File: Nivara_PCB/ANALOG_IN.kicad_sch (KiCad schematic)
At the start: 0 parts

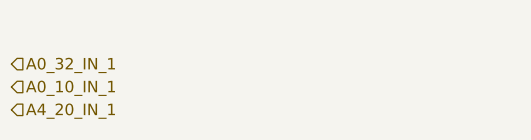
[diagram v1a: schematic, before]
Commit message: Añadido de funciones NPN/PNP
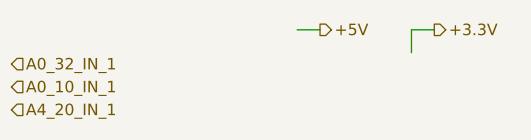
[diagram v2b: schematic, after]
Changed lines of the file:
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@@
 	(generator_version "9.0")
 	(paper "A4")
+	(wire
+		(pts
+			(xy 86.36 52.07) (xy 88.9 52.07)
+		)
+		(stroke
+			(width 0)
+			(type default)
+		)
+	)
+	(wire
+		(pts
+			(xy 101.6 52.07) (xy 99.06 52.07)
+		)
+		(stroke
+			(width 0)
+			(type default)
+		)
+	)
+	(wire
+		(pts
+			(xy 99.06 52.07) (xy 99.06 54.61)
+		)
+		(stroke
+			(width 0)
+			(type default)
+		)
+	)
+	(hierarchical_label "+3.3V"
+		(shape output)
+		(at 101.6 52.07 0)
+		(effects
+			(font
+				(size 1.27 1.27)
+			)
+			(justify left)
+		)
+	)
+	(hierarchical_label "+5V"
+		(shape output)
+		(at 88.9 52.07 0)
+		(effects
+			(font
+				(size 1.27 1.27)
+			)
+			(justify left)
+		)
+	)
 	(hierarchical_label "A4_20_IN_1"
 		(shape input)

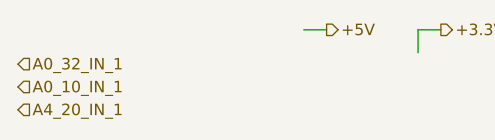
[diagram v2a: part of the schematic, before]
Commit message: Cambios en el esquema de NPN y PNP
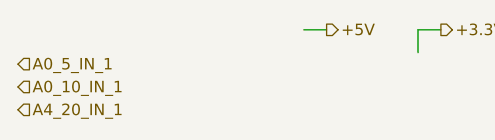
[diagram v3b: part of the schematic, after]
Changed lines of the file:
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@@
 		)
 	)
-	(hierarchical_label "A0_32_IN_1"
+	(hierarchical_label "A0_5_IN_1"
 		(shape input)
 		(at 54.61 55.88 0)

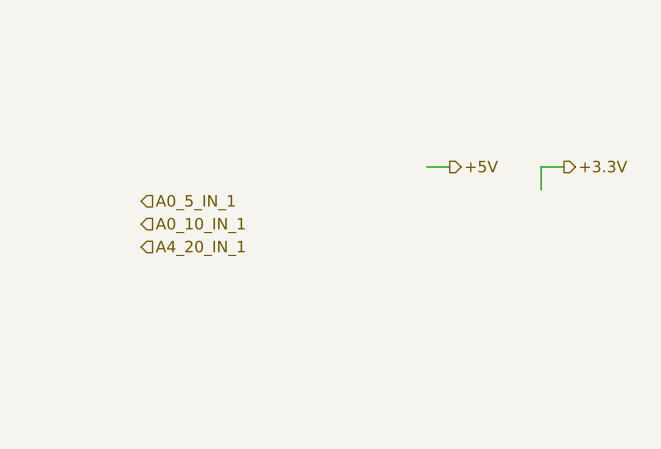
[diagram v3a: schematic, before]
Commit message: Cambios en las mediciones análogas.
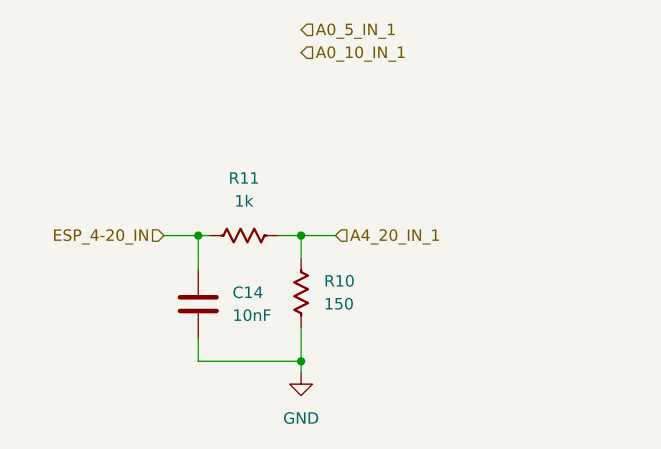
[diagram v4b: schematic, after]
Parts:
- added C14: 10nF, PCM_Capacitor_SMD_AKL:C_0603_1608Metric, symbol PCM_Capacitor_US_AKL:C_0603
- added R10: 150, PCM_Resistor_SMD_AKL:R_0805_2012Metric, symbol PCM_Resistor_US_AKL:R_0805
- added R11: 1k, PCM_Resistor_SMD_AKL:R_0603_1608Metric, symbol PCM_Resistor_US_AKL:R_0603
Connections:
- net A4_20_IN_1: now also R10.1, R11.2
- new net ESP_4-20_IN: C14.1, R11.1
- new net GND: C14.2, R10.2

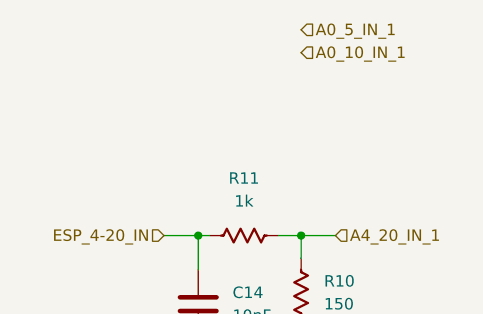
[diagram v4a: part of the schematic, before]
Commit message: Cambios en las salidas analogicas, ya que el ESP32 S3 no tiene DAC
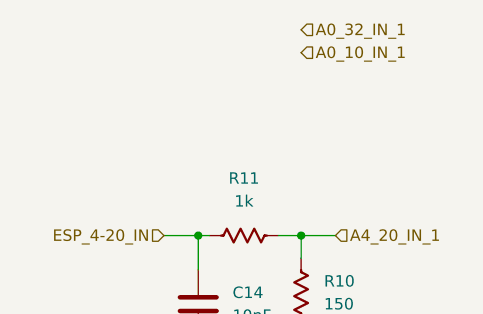
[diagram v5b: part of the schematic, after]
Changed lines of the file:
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@@
 		)
 	)
-	(hierarchical_label "A0_5_IN_1"
+	(hierarchical_label "A0_32_IN_1"
 		(shape input)
 		(at 72.39 36.83 0)

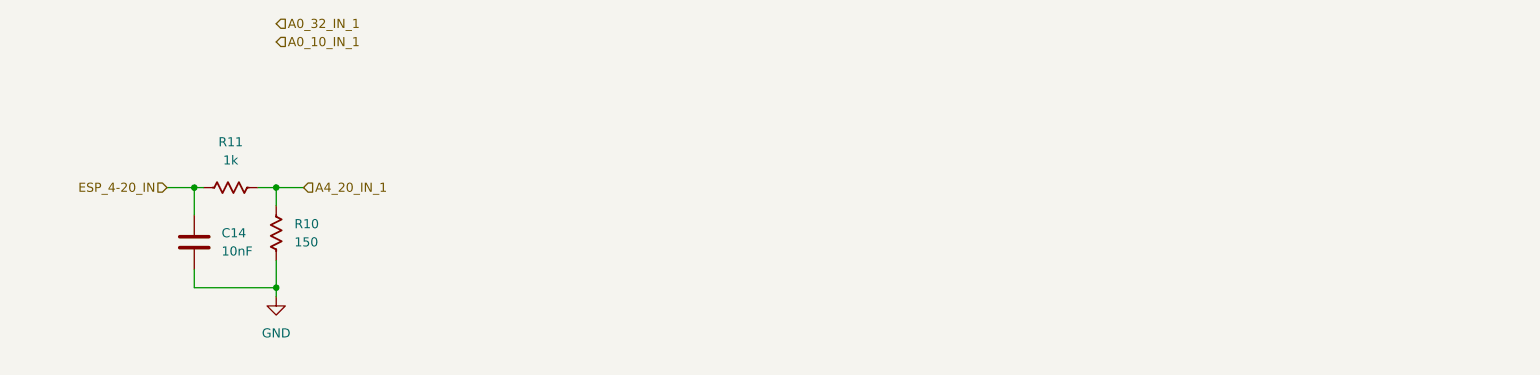
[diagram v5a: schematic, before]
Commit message: Cambios en la medición de voltaje y corriente de la PCB Nivara.
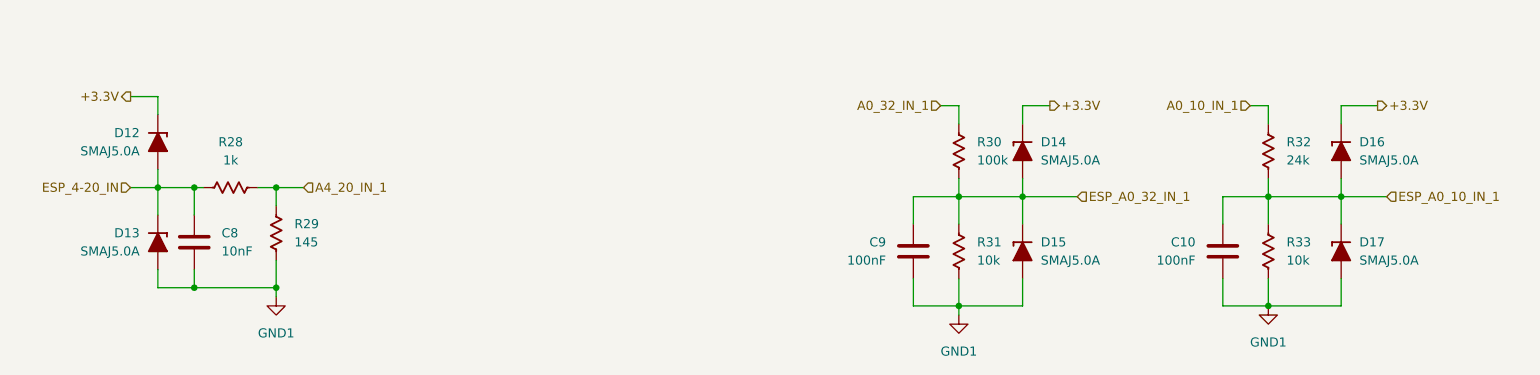
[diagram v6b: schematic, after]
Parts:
- added C10, C9: 100nF, PCM_Capacitor_SMD_AKL:C_0603_1608Metric, symbol PCM_Capacitor_US_AKL:C_0603
- added D12, D13, D14, D15, D16, D17: SMAJ5.0A, PCM_Diode_SMD_AKL:D_SMA, symbol PCM_Diode_TVS_AKL:SMAJ5.0A
- added R30: 100k, PCM_Resistor_SMD_AKL:R_0603_1608Metric, symbol PCM_Resistor_US_AKL:R_0603
- added R31, R33: 10k, PCM_Resistor_SMD_AKL:R_0603_1608Metric, symbol PCM_Resistor_US_AKL:R_0603
- added R32: 24k, PCM_Resistor_SMD_AKL:R_0603_1608Metric, symbol PCM_Resistor_US_AKL:R_0603
- C8: renamed from C14; Voltage (none) -> 10V
- R29: renamed from R10; value 150 -> 145
- renumbered R11 to R28
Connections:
- net A0_10_IN_1: now also R32.2
- net A0_32_IN_1: now also R30.2
- net ESP_4-20_IN: now also D12.2 (A), D13.1 (K)
- net GND renamed GND1
- net GND1: now also C10.2, C9.2, D13.2 (A), D15.2 (A), D17.2 (A), R31.1, R33.1
- new net +3.3V: D12.1 (K), D14.1 (K), D16.1 (K)
- new net ESP_A0_10_IN_1: C10.1, D16.2 (A), D17.1 (K), R32.1, R33.2
- new net ESP_A0_32_IN_1: C9.1, D14.2 (A), D15.1 (K), R30.1, R31.2

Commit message: Cambios en el PCB de Nivara. Ruteo de emtradas y salidas NPN y PNP.
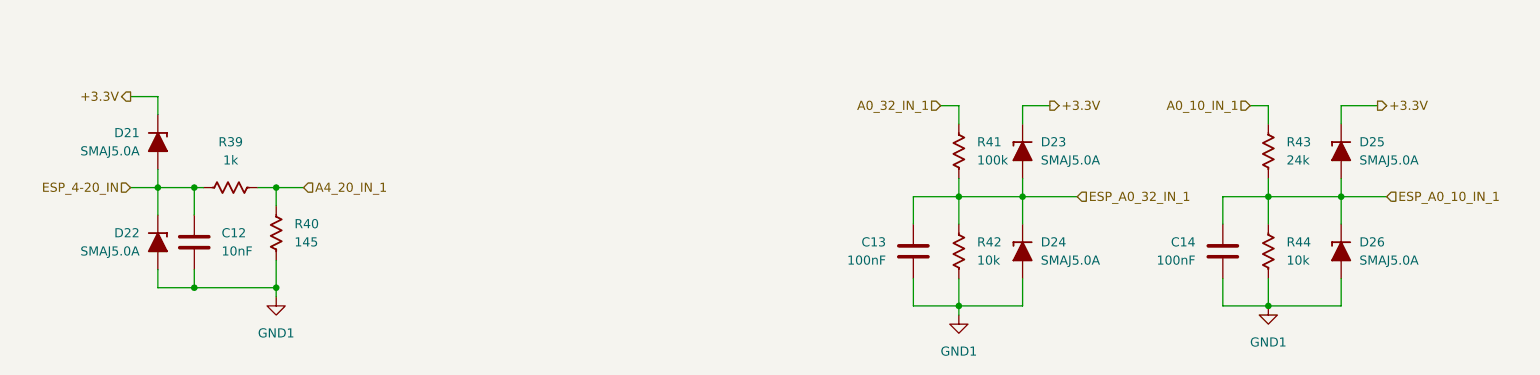
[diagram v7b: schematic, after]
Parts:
- renumbered C8 to C12, C9 to C13, C10 to C14, D12 to D21, D13 to D22, D14 to D23, D15 to D24, D16 to D25, D17 to D26, R28 to R39, R29 to R40, R30 to R41, R31 to R42, R32 to R43, R33 to R44
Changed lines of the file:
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@@
 		(dnp no)
 		(fields_autoplaced yes)
-		(property "Reference" "D17"
+		(property "Reference" "D26"
 			(at 223.52 67.3099 90)
 			(effects
@@
 			(project "Nivara_PCB"
 				(path "/13184db0-a71d-4054-b13a-bbf46d2b100d/4e7fa7f2-8bf5-4f9c-874d-fa1b4fd76f92/20ba0c48-a9e2-46df-b6c2-3a15a589565c"
-					(reference "D17")
+					(reference "D26")
 					(unit 1)
 				)
@@
 		(dnp no)
 		(fields_autoplaced yes)
-		(property "Reference" "C8"
+		(property "Reference" "C12"
 			(at 64.77 66.0399 0)
 			(effects
@@
 			(project ""
 				(path "/13184db0-a71d-4054-b13a-bbf46d2b100d/4e7fa7f2-8bf5-4f9c-874d-fa1b4fd76f92/20ba0c48-a9e2-46df-b6c2-3a15a589565c"
-					(reference "C8")
+					(reference "C12")
 					(unit 1)
 				)
@@
 		(dnp no)
 		(fields_autoplaced yes)
-		(property "Reference" "R29"
+		(property "Reference" "R40"
 			(at 74.93 64.7699 0)
 			(effects
@@
 			(project ""
 				(path "/13184db0-a71d-4054-b13a-bbf46d2b100d/4e7fa7f2-8bf5-4f9c-874d-fa1b4fd76f92/20ba0c48-a9e2-46df-b6c2-3a15a589565c"
-					(reference "R29")
+					(reference "R40")
 					(unit 1)
 				)
@@
 		(dnp no)
 		(fields_autoplaced yes)
-		(property "Reference" "D16"
+		(property "Reference" "D25"
 			(at 223.52 53.3399 90)
 			(effects
@@
 			(project "Nivara_PCB"
 				(path "/13184db0-a71d-4054-b13a-bbf46d2b100d/4e7fa7f2-8bf5-4f9c-874d-fa1b4fd76f92/20ba0c48-a9e2-46df-b6c2-3a15a589565c"
-					(reference "D16")
+					(reference "D25")
 					(unit 1)
 				)
@@
 		(dnp no)
 		(fields_autoplaced yes)
-		(property "Reference" "D13"
+		(property "Reference" "D22"
 			(at 53.34 66.0399 90)
 			(effects
@@
 			(project "Nivara_PCB"
 				(path "/13184db0-a71d-4054-b13a-bbf46d2b100d/4e7fa7f2-8bf5-4f9c-874d-fa1b4fd76f92/20ba0c48-a9e2-46df-b6c2-3a15a589565c"
-					(reference "D13")
+					(reference "D22")
 					(unit 1)
 				)
@@
 		(dnp no)
 		(fields_autoplaced yes)
-		(property "Reference" "D14"
+		(property "Reference" "D23"
 			(at 179.07 53.3399 90)
 			(effects
@@
 			(project "Nivara_PCB"
 				(path "/13184db0-a71d-4054-b13a-bbf46d2b100d/4e7fa7f2-8bf5-4f9c-874d-fa1b4fd76f92/20ba0c48-a9e2-46df-b6c2-3a15a589565c"
-					(reference "D14")
+					(reference "D23")
 					(unit 1)
 				)
@@
 		(dnp no)
 		(fields_autoplaced yes)
-		(property "Reference" "D12"
+		(property "Reference" "D21"
 			(at 53.34 52.0699 90)
 			(effects
@@
 			(project "Nivara_PCB"
 				(path "/13184db0-a71d-4054-b13a-bbf46d2b100d/4e7fa7f2-8bf5-4f9c-874d-fa1b4fd76f92/20ba0c48-a9e2-46df-b6c2-3a15a589565c"
-					(reference "D12")
+					(reference "D21")
 					(unit 1)
 				)
@@
 		(dnp no)
 		(fields_autoplaced yes)
-		(property "Reference" "R28"
+		(property "Reference" "R39"
 			(at 66.04 53.34 90)
 			(effects
@@
 			(project ""
 				(path "/13184db0-a71d-4054-b13a-bbf46d2b100d/4e7fa7f2-8bf5-4f9c-874d-fa1b4fd76f92/20ba0c48-a9e2-46df-b6c2-3a15a589565c"
-					(reference "R28")
+					(reference "R39")
 					(unit 1)
 				)
@@
 		(on_board yes)
 		(dnp no)
-		(property "Reference" "C10"
+		(property "Reference" "C14"
 			(at 200.66 67.3099 0)
 			(effects
@@
 			(project "Nivara_PCB"
 				(path "/13184db0-a71d-4054-b13a-bbf46d2b100d/4e7fa7f2-8bf5-4f9c-874d-fa1b4fd76f92/20ba0c48-a9e2-46df-b6c2-3a15a589565c"
-					(reference "C10")
+					(reference "C14")
 					(unit 1)
 				)
@@
 		(dnp no)
 		(fields_autoplaced yes)
-		(property "Reference" "R32"
+		(property "Reference" "R43"
 			(at 213.36 53.3399 0)
 			(effects
@@
 			(project "Nivara_PCB"
 				(path "/13184db0-a71d-4054-b13a-bbf46d2b100d/4e7fa7f2-8bf5-4f9c-874d-fa1b4fd76f92/20ba0c48-a9e2-46df-b6c2-3a15a589565c"
-					(reference "R32")
+					(reference "R43")
 					(unit 1)
 				)
@@
 		(dnp no)
 		(fields_autoplaced yes)
-		(property "Reference" "D15"
+		(property "Reference" "D24"
 			(at 179.07 67.3099 90)
 			(effects
@@
 			(project ""
 				(path "/13184db0-a71d-4054-b13a-bbf46d2b100d/4e7fa7f2-8bf5-4f9c-874d-fa1b4fd76f92/20ba0c48-a9e2-46df-b6c2-3a15a589565c"
-					(reference "D15")
+					(reference "D24")
 					(unit 1)
 				)
@@
 		(dnp no)
 		(fields_autoplaced yes)
-		(property "Reference" "#PWR045"
+		(property "Reference" "#PWR066"
 			(at 210.82 82.55 0)
 			(effects
@@
 			(project "Nivara_PCB"
 				(path "/13184db0-a71d-4054-b13a-bbf46d2b100d/4e7fa7f2-8bf5-4f9c-874d-fa1b4fd76f92/20ba0c48-a9e2-46df-b6c2-3a15a589565c"
-					(reference "#PWR045")
+					(reference "#PWR066")
 					(unit 1)
 				)
@@
 		(dnp no)
 		(fields_autoplaced yes)
-		(property "Reference" "R31"
+		(property "Reference" "R42"
 			(at 170.18 67.3099 0)
 			(effects
@@
 			(project "Nivara_PCB"
 				(path "/13184db0-a71d-4054-b13a-bbf46d2b100d/4e7fa7f2-8bf5-4f9c-874d-fa1b4fd76f92/20ba0c48-a9e2-46df-b6c2-3a15a589565c"
-					(reference "R31")
+					(reference "R42")
 					(unit 1)
 				)
@@
 		(dnp no)
 		(fields_autoplaced yes)
-		(property "Reference" "#PWR044"
+		(property "Reference" "#PWR065"
 			(at 167.64 83.82 0)
 			(effects
@@
 			(project "Nivara_PCB"
 				(path "/13184db0-a71d-4054-b13a-bbf46d2b100d/4e7fa7f2-8bf5-4f9c-874d-fa1b4fd76f92/20ba0c48-a9e2-46df-b6c2-3a15a589565c"
-					(reference "#PWR044")
+					(reference "#PWR065")
 					(unit 1)
 				)
@@
 		(dnp no)
 		(fields_autoplaced yes)
-		(property "Reference" "#PWR043"
+		(property "Reference" "#PWR064"
 			(at 72.39 81.28 0)
 			(effects
@@
 			(project ""
 				(path "/13184db0-a71d-4054-b13a-bbf46d2b100d/4e7fa7f2-8bf5-4f9c-874d-fa1b4fd76f92/20ba0c48-a9e2-46df-b6c2-3a15a589565c"
-					(reference "#PWR043")
+					(reference "#PWR064")
 					(unit 1)
 				)
@@
 		(dnp no)
 		(fields_autoplaced yes)
-		(property "Reference" "R30"
+		(property "Reference" "R41"
 			(at 170.18 53.3399 0)
 			(effects
@@
 			(project "Nivara_PCB"
 				(path "/13184db0-a71d-4054-b13a-bbf46d2b100d/4e7fa7f2-8bf5-4f9c-874d-fa1b4fd76f92/20ba0c48-a9e2-46df-b6c2-3a15a589565c"
-					(reference "R30")
+					(reference "R41")
 					(unit 1)
 				)
@@
 		(dnp no)
 		(fields_autoplaced yes)
-		(property "Reference" "R33"
+		(property "Reference" "R44"
 			(at 213.36 67.3099 0)
 			(effects
@@
 			(project "Nivara_PCB"
 				(path "/13184db0-a71d-4054-b13a-bbf46d2b100d/4e7fa7f2-8bf5-4f9c-874d-fa1b4fd76f92/20ba0c48-a9e2-46df-b6c2-3a15a589565c"
-					(reference "R33")
+					(reference "R44")
 					(unit 1)
 				)
@@
 		(on_board yes)
 		(dnp no)
-		(property "Reference" "C9"
+		(property "Reference" "C13"
 			(at 157.48 67.3099 0)
 			(effects
@@
 			(project "Nivara_PCB"
 				(path "/13184db0-a71d-4054-b13a-bbf46d2b100d/4e7fa7f2-8bf5-4f9c-874d-fa1b4fd76f92/20ba0c48-a9e2-46df-b6c2-3a15a589565c"
-					(reference "C9")
-					(unit 1)
-				)
+					(reference "C13")
+					(unit 1)
+				)
